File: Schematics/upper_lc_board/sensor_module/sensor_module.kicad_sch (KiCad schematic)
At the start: 39 parts, among them J2 HAL_SENS, J3 PT1, J4 PT2, J7 TC, U10 OA-TLV9001IDCK, U11 OA-TLV9001IDCK, U7 ADC_ADS131M04IPWR, U9 OA-TLV9001IDCK

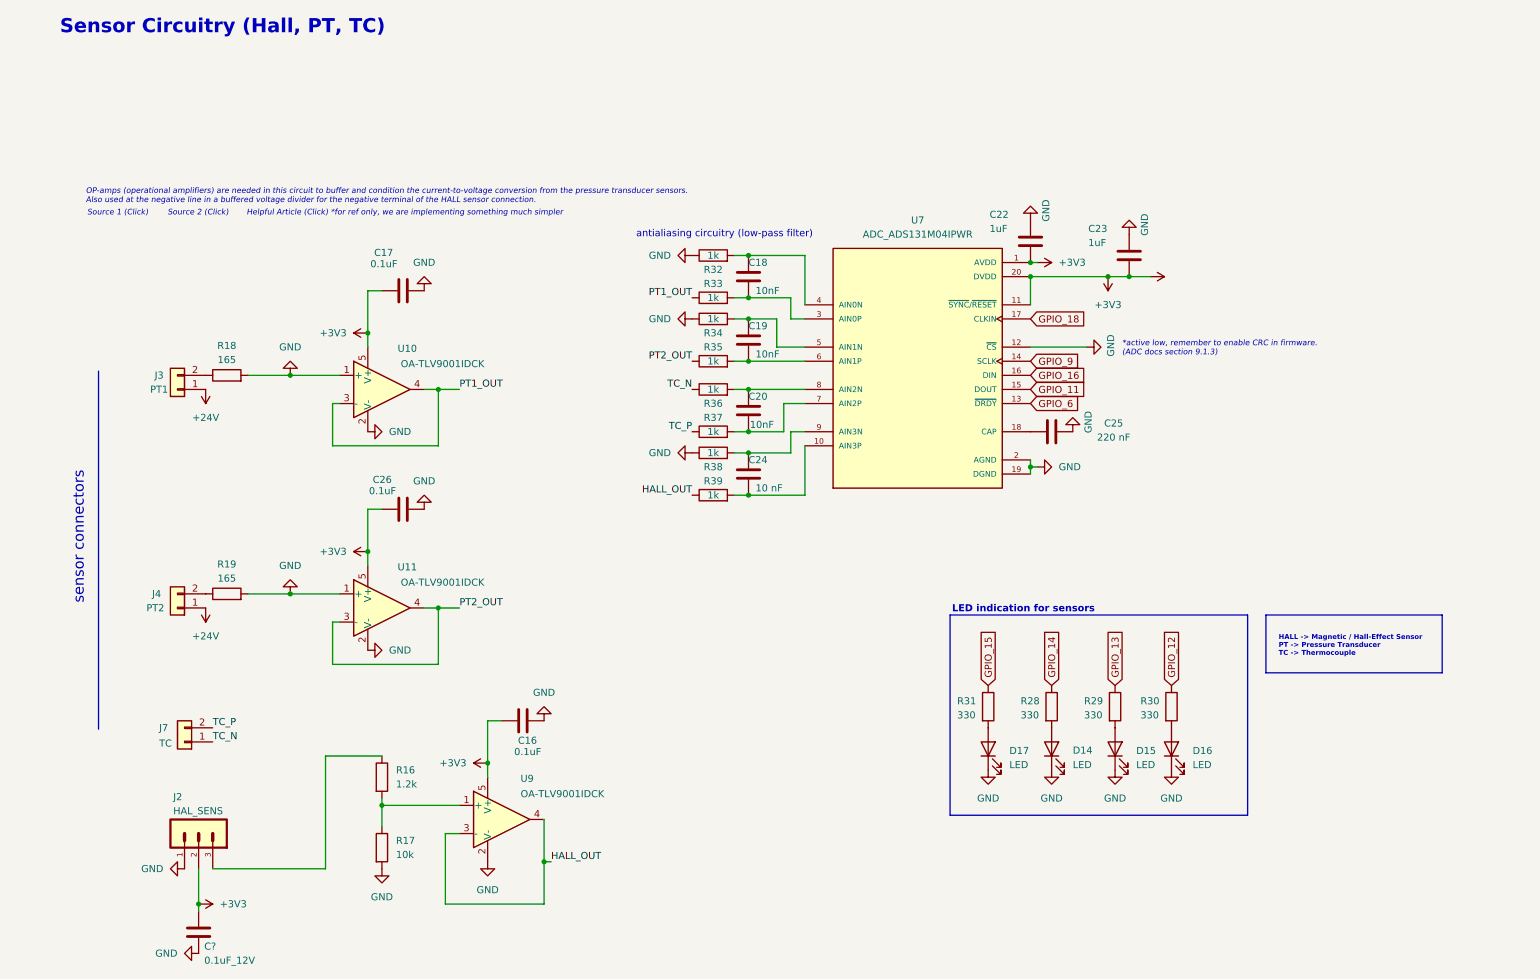
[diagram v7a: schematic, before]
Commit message: add TC circuitry; finish layout next.
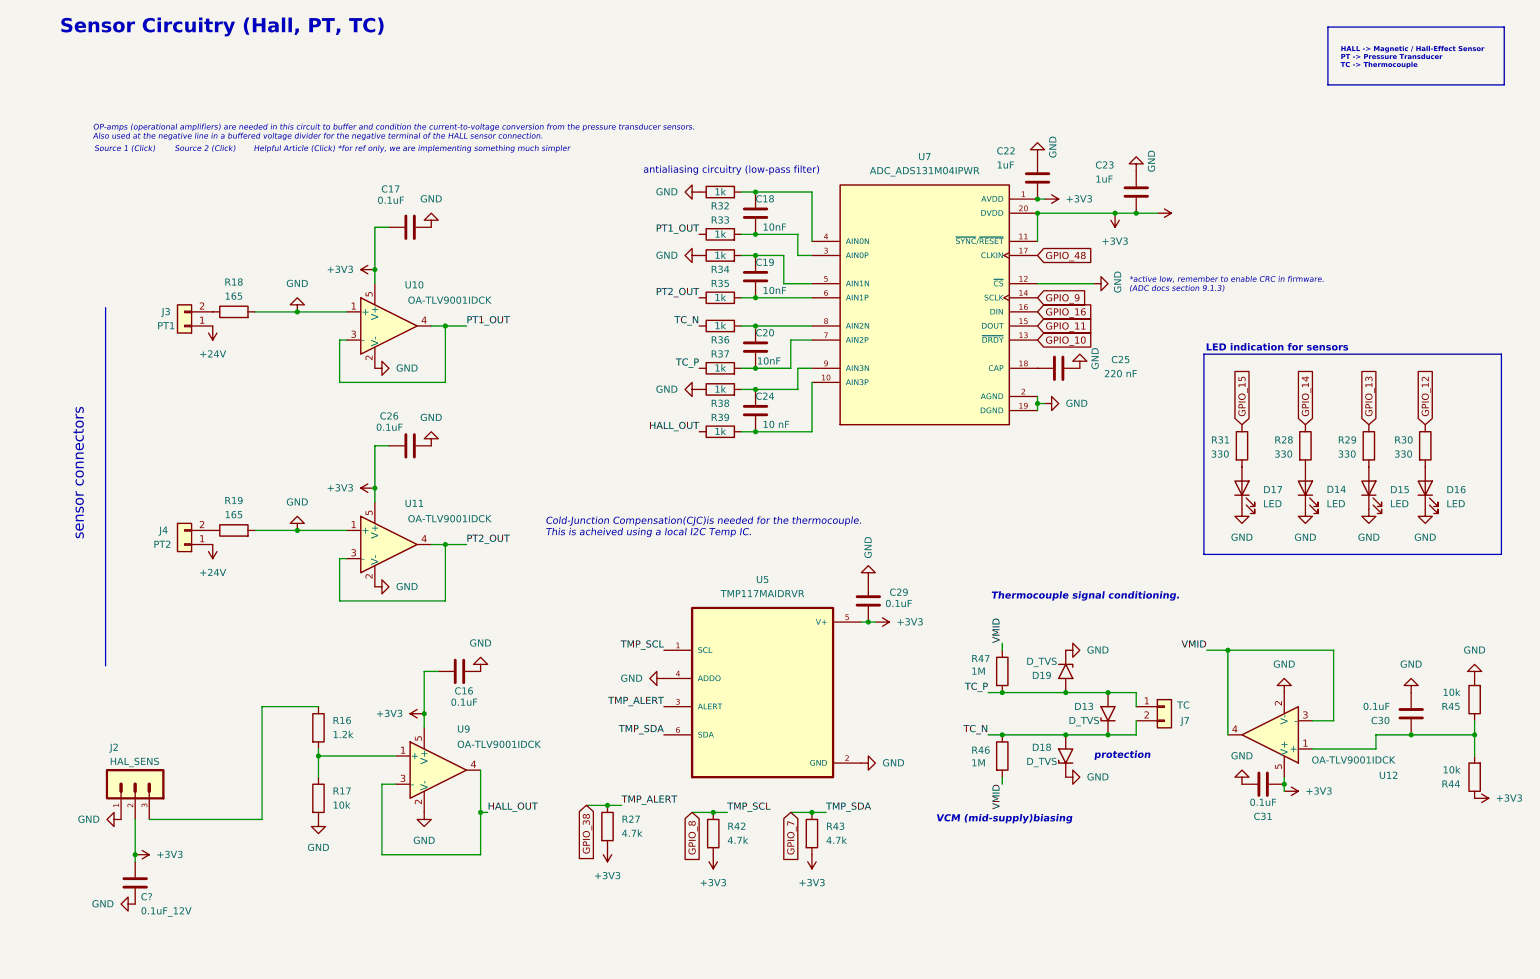
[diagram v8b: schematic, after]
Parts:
- added C29: 0.1uF, Capacitor_SMD:C_0603_1608Metric, symbol Device:C
- added C30, C31: 0.1uF, symbol Device:C
- added D13, D18, D19: D_TVS, SMBJ28A:DIOM5436X244N, symbol Diode:1.5KExxA
- added R27, R42, R43: 4.7k, symbol Device:R
- added R44, R45: 10k, symbol Device:R
- added R46, R47: 1M, symbol Device:R
- added U12: OA-TLV9001IDCK, Package_TO_SOT_SMD:SOT-353_SC-70-5, symbol Amplifier_Operational:TLV9001IDCK
- added U5: TMP117MAIDRVR, TMP117MAIDRVR:SON65P200X200X80-7N, symbol TMP117MAIDRVR:TMP117MAIDRVR
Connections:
- net +3V3: now also C29.2, C31.1, R27.2, R42.2, R43.2, R44.1, U12.5 (V+), U5.5 (V+)
- net GND: now also C29.1, C30.2, C31.2, D18.1 (A1), D19.1 (A1), R45.2, U12.2 (V-), U5.2 (GND), U5.4 (ADDO)
- net TC_N: now also J7.2 (Pin_2), D13.1 (A1), D18.2 (A2), R46.1; no longer J7.1 (Pin_1)
- net TC_P: now also J7.1 (Pin_1), D13.2 (A2), D19.2 (A2), R47.2; no longer J7.2 (Pin_2)
- net GPIO_18 renamed GPIO_48
- net GPIO_6 renamed GPIO_10
- new net: C30.1, R44.2, R45.1, U12.1 (+)
- new net GPIO_38: R27.1, U5.3 (ALERT)
- new net GPIO_7: R43.1, U5.6 (SDA)
- new net GPIO_8: R42.1, U5.1 (SCL)
- new net VMID: R46.2, R47.1, U12.3 (-), U12.4
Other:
- note added: "Cold-Junction Compensation(CJC)is needed for the thermocouple. This is acheived using a local I2C Temp IC."
- note added: "Thermocouple signal conditioning."
- note added: "VCM (mid-supply)biasing"
- note added: "protection"
- moved on the sheet: C16, C17, C18, C19, C20, C22, C23, C24, C25, C26, C?, D14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
